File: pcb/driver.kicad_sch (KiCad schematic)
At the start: 43 parts

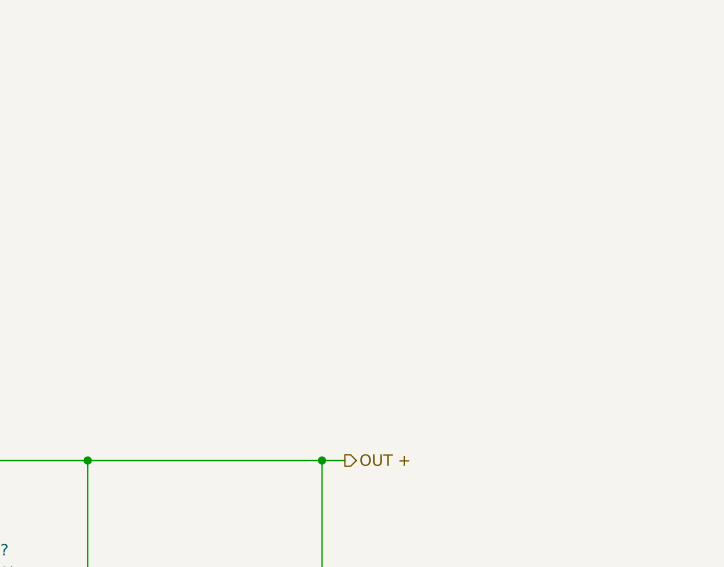
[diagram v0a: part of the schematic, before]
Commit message: Added some design hints
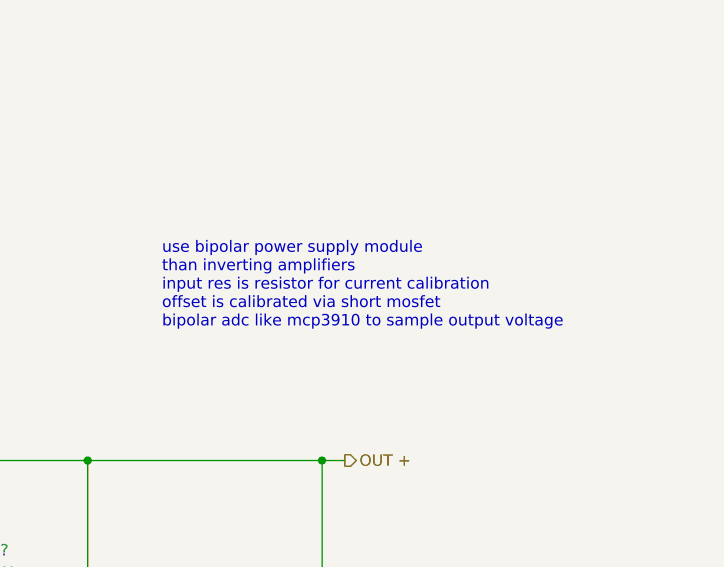
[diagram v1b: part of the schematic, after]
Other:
- note added: "use bipolar power supply module than inverting amplifiers input res is resistor for current calibration offset is calibrated via short mosfet bipolar adc like mcp3910 to sample output voltage"
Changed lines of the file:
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@@
+    (effects (font (size 1.27 1.27)) (justify left bottom))
+  )
+  (text "use bipolar power supply module\nthan inverting amplifiers\ninput res is resistor for current calibration\noffset is calibrated via short mosfet\nbipolar adc like mcp3910 to sample output voltage"
+    (at 249.555 64.135 0)
     (effects (font (size 1.27 1.27)) (justify left bottom))
   )

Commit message: updated schematics for bipolar supply of opamps
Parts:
- removed C?: 100n, symbol Device:C
- removed D?: BAV99, Package_TO_SOT_SMD:SOT-23, symbol Diode:BAV99
- removed D?: BZX84C3V3LT1G, Package_TO_SOT_SMD:SOT-23, symbol Diode:BZX84Cxx
- removed Q?: BC847, Package_TO_SOT_SMD:SOT-23, symbol Transistor_BJT:BC847
- removed Q? (x2): DMN2056U, Package_TO_SOT_SMD:SOT-23, symbol Transistor_FET:DMN2056U
- removed R? (x7): 10k .1%, symbol Device:R
- removed R? (x3): 10k, symbol Device:R
- removed R? (x2): R, symbol Device:R
- removed R?: 3.3 2W, symbol Device:R
- removed R? (x3): 100k .1%, symbol Device:R
- removed R?: 82, symbol Device:R
- removed U?: SN74AXC1T45, symbol zz_Logic_LevelTranslator:SN74AXC1T45
- removed U? (x3): LM358, symbol Amplifier_Operational:LM358
- added C? (x2): 220n, symbol Device:C
- added C?: 47n, symbol Device:C
- added Q?: BC847, Package_TO_SOT_SMD:SOT-23, symbol Transistor_BJT:BC847
- added Q?: DMN2056U, Package_TO_SOT_SMD:SOT-23, symbol Transistor_FET:DMN2056U
- added R? (x2): 220, symbol Device:R
- added R?: R, symbol Device:R
- added R?: 3.3 2W, symbol Device:R
- added RN? (x8): 10k 0.05%, symbol Device:R_Pack04_Split
- added U? (x3): OP07, symbol Amplifier_Operational:OP07
- added U? (x3): LM358, symbol Amplifier_Operational:LM358
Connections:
- net CC REF: now also R?.1; no longer R?.2
- net CV REF: now also R?.1; no longer R?.2
- net GND: now also C?.2, C?.2, C?.2, Q?.2 (E), Q?.2 (S), U?.3 (+), U?.3 (+); no longer C?.2, U?.4 (V-)
- net short: now also Q?.1 (G), R?.1
- net at D?.3 (K), Q?.1 (B), R?.1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: now also Q?.3 (C)
- net C MEAS: now reaches R?.2
- net C MEAS: now also RN?.4 (R4.1), U?.6
- net at D?.2 (A), Q?.3 (E), R?.2: now also R?.1, RN?.7 (R2.2)
- net at C?.1, R?.2: now also U?.6
- net at R?.1: now also U?.2 (-)
- net at C?.2, R?.1: now also U?.3 (+)
- net +12V renamed VIN
- net VIN: no longer C?.1, U?.8 (V+)
- net V MEAS+ renamed V MEAS
- net V MEAS: now also RN?.2 (R2.1), RN?.4 (R4.1), RN?.6 (R3.2), U?.6
- new net: RN?.1 (R1.1), RN?.5 (R4.2)
- new net: RN?.2 (R2.1), RN?.3 (R3.1), RN?.8 (R1.2), U?.2 (-)
- new net: C?.1, R?.2, U?.5 (+)
- new net: R?.2, U?.1, U?.2 (-)
- new net: C?.1, R?.2, U?.3 (+)
- new net: R?.2, U?.6 (-), U?.7
- new net: RN?.1 (R1.1), RN?.3 (R3.1), RN?.5 (R4.2), RN?.7 (R2.2), U?.2 (-)
- new net: Q?.1 (B), R?.2
- new net VN: C?.2, U?.4 (V-), U?.4 (V-), U?.4 (V-), U?.4 (V-), U?.4 (V-)
- new net VOUT: C?.1, Q?.3 (D), R?.2, RN?.6 (R3.2), RN?.8 (R1.2)
- new net VP: C?.1, U?.7 (V+), U?.7 (V+), U?.7 (V+), U?.8 (V+), U?.8 (V+)
- no-connect marks 2 -> 1
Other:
- note added: "ACAS 0612"
- note added: "alternate paralleling for better tempco"
- note added: "best matching for input resistors"
- note added: "could control with 2 bits: comm -> oe and short inverter dir -> short inverter and dir but this could cause issues at calibration or with driven output of lvl shifter"
- note added: "dir short oe tx 1 0 1 rx 0 0 1 sup 0 0 0 shrt 0 1 1"
- note added: "low impedance"
- note removed: "DIR short oe tx 1 0 1 rx 0 0 1 sup 0 0 0 shrt 0 1 1"
- note removed: "LM358 / TLV9102 / TLV9152 / TLV9162 pin compatible"
- note removed: "SN74AXC1T45 - 82 Ohm + zener diode + diode to vdd -V"
- note removed: "current too low"
- note removed: "dont really like this because of offset with common mode input and output drive range when V~0"
- note removed: "or ldo/opamp with npn + resistor ~150ohm to gnd"
- note removed: "protect IOs if wrong direction"
- moved on the sheet: C?, D?, Q?, R?, U?A, U?C
